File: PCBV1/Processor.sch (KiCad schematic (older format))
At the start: 41 parts

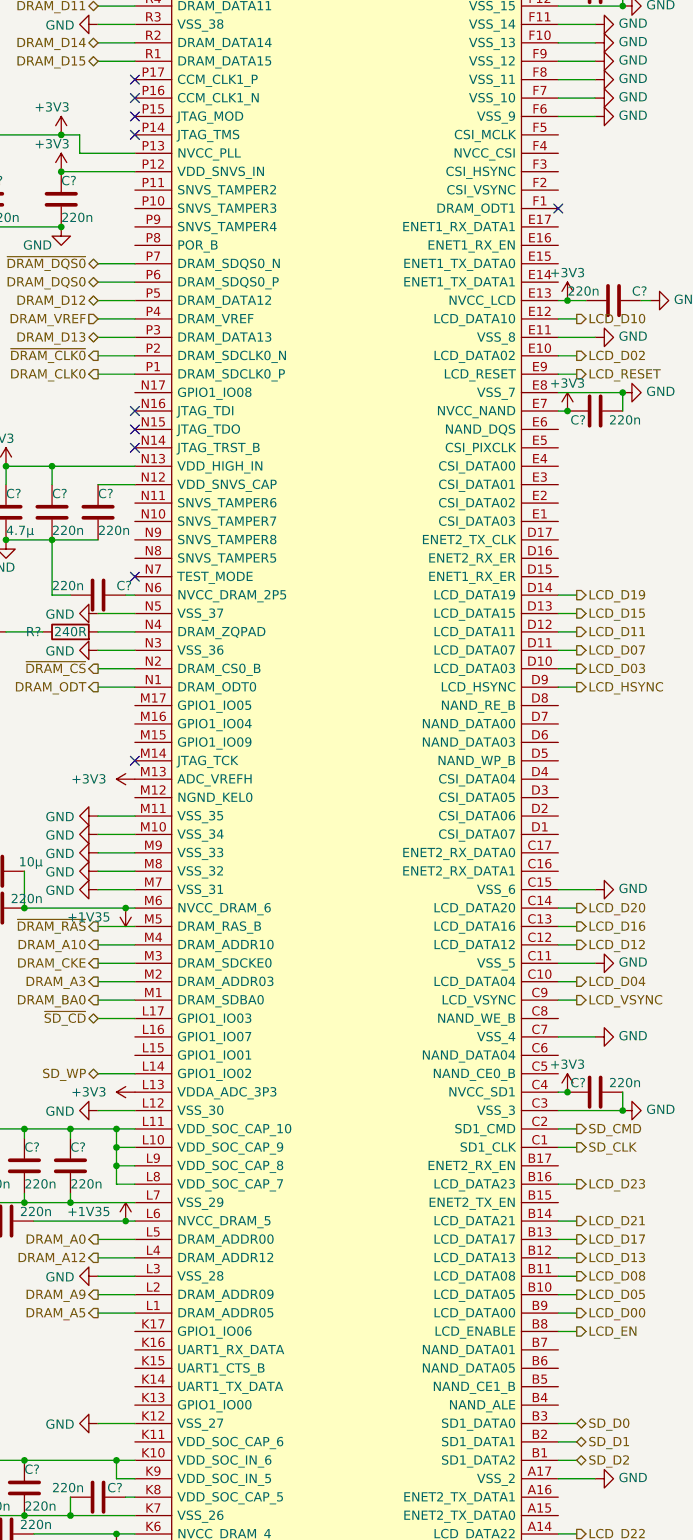
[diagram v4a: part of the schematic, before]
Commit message: Added SD filter and USB-to-UART IC.
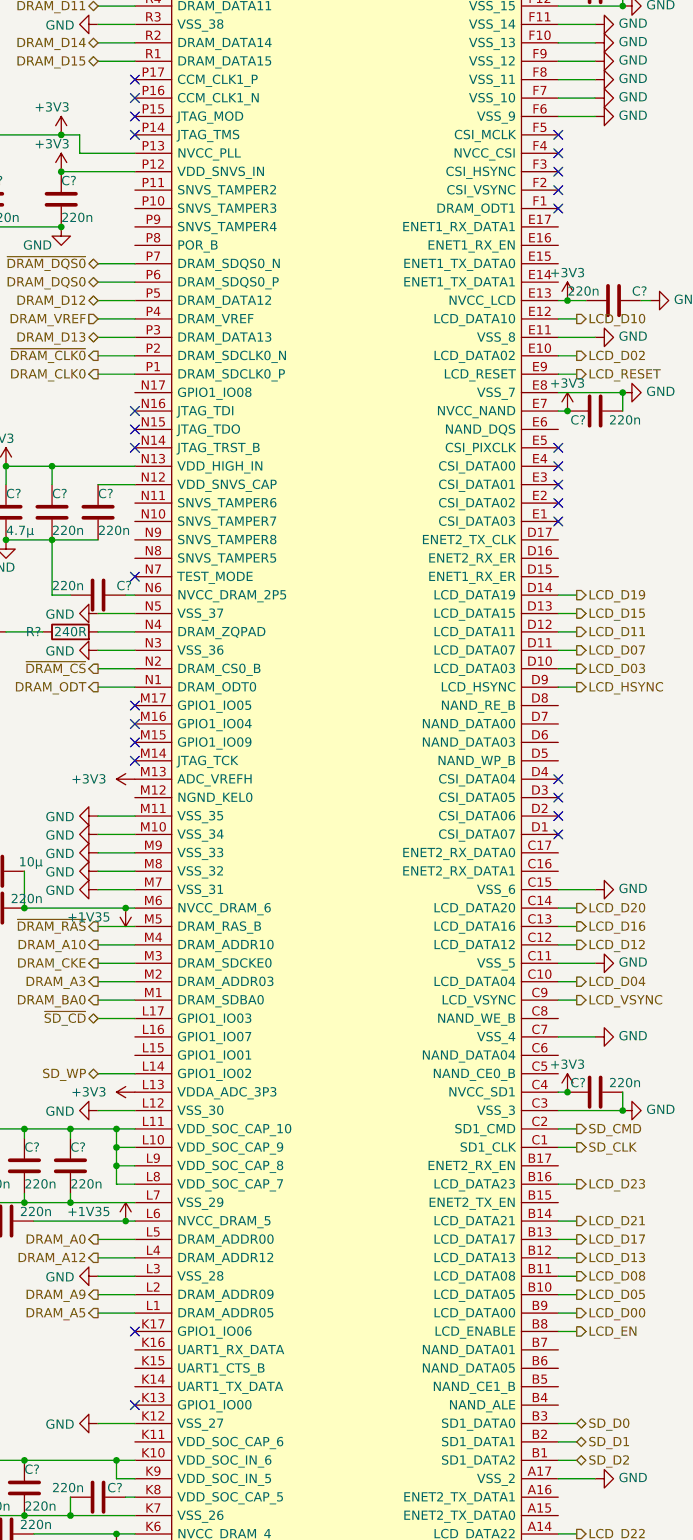
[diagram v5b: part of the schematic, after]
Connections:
- no-connect marks 21 -> 39
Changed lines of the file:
@@
 $Descr A3 11693 16535 portrait
 encoding utf-8
-Sheet 8 8
+Sheet 7 8
 Title "Smart Mirror"
-Date "2021-01-21"
+Date "2022-04-22"
 Rev "1.0"
 Comp "University of Southern Denmark"
@@
 	5150 7650 5050 7650
 NoConn ~ 5050 6750
+NoConn ~ 5050 10150
+NoConn ~ 5050 10050
+NoConn ~ 5050 9950
+NoConn ~ 5050 9850
+NoConn ~ 5050 8450
+NoConn ~ 5050 8350
+NoConn ~ 5050 8250
+NoConn ~ 5050 8150
+NoConn ~ 5050 8050
+NoConn ~ 5050 6650
+NoConn ~ 5050 6550
+NoConn ~ 5050 6450
+NoConn ~ 5050 6350
+NoConn ~ 2750 9450
+NoConn ~ 2750 9550
+NoConn ~ 2750 9650
+NoConn ~ 2750 13250
+NoConn ~ 2750 12850
 $EndSCHEMATC

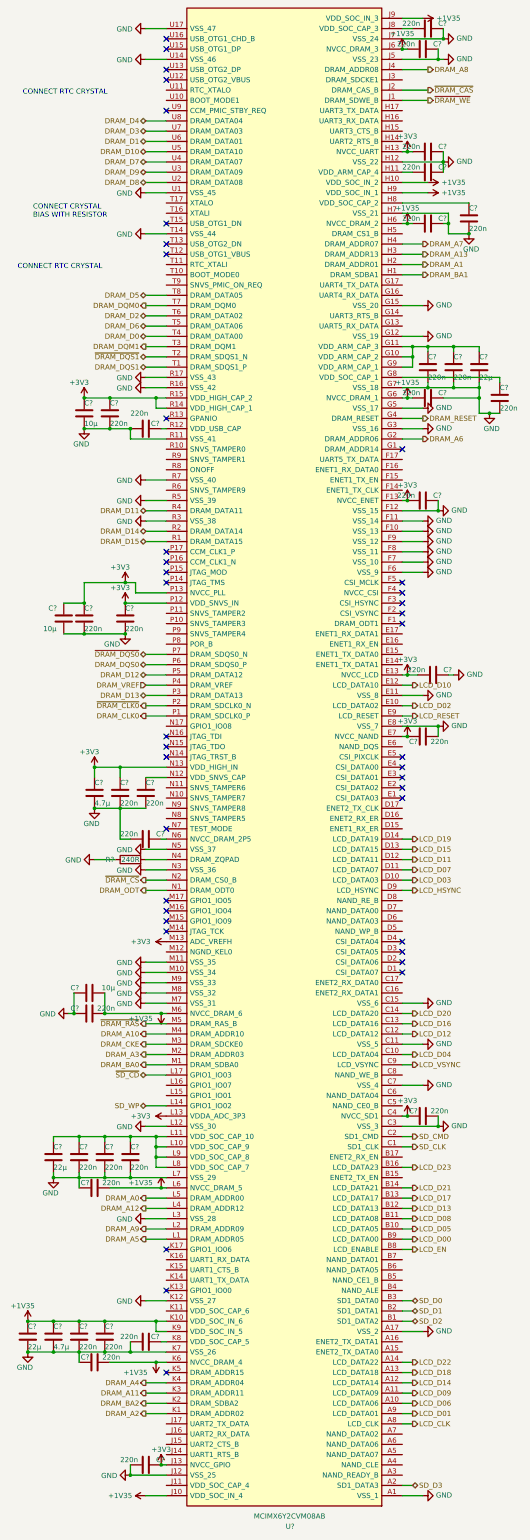
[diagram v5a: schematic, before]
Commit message: Many minor changes to component footprints and schematics.
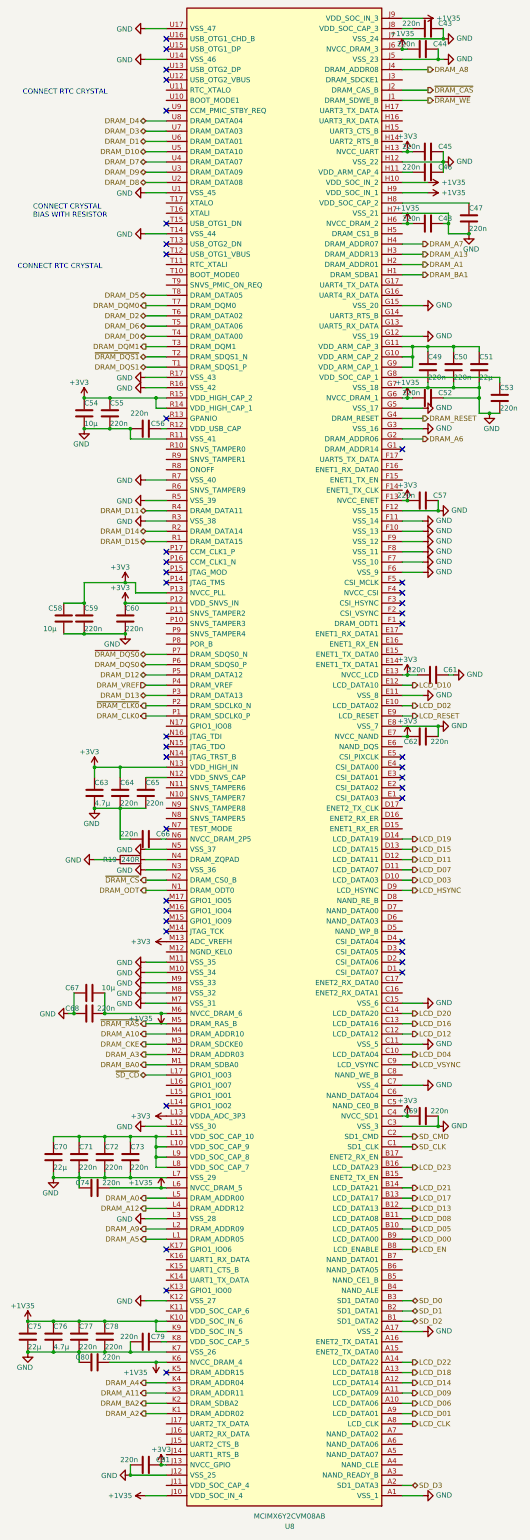
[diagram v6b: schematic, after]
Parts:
- C43, C44, C45, C46, C47, C48, C49, C50, C52, C53, C55, C56, C57, C59, C60, C61, C62, C64, C65, C66, C68, C69, C71, C72, C73, C74, C76, C77, C78, C79, C80, C81: renamed from C?; footprint (none) -> Capacitor_SMD:C_0603_1608Metric
- R19: renamed from R?; footprint (none) -> Resistor_SMD:R_0603_1608Metric
- gave numbers to parts that had none: 8
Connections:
- net SD_WP: no longer names the net of U8.L14 (GPIO1_IO02)
- no-connect marks 39 -> 40

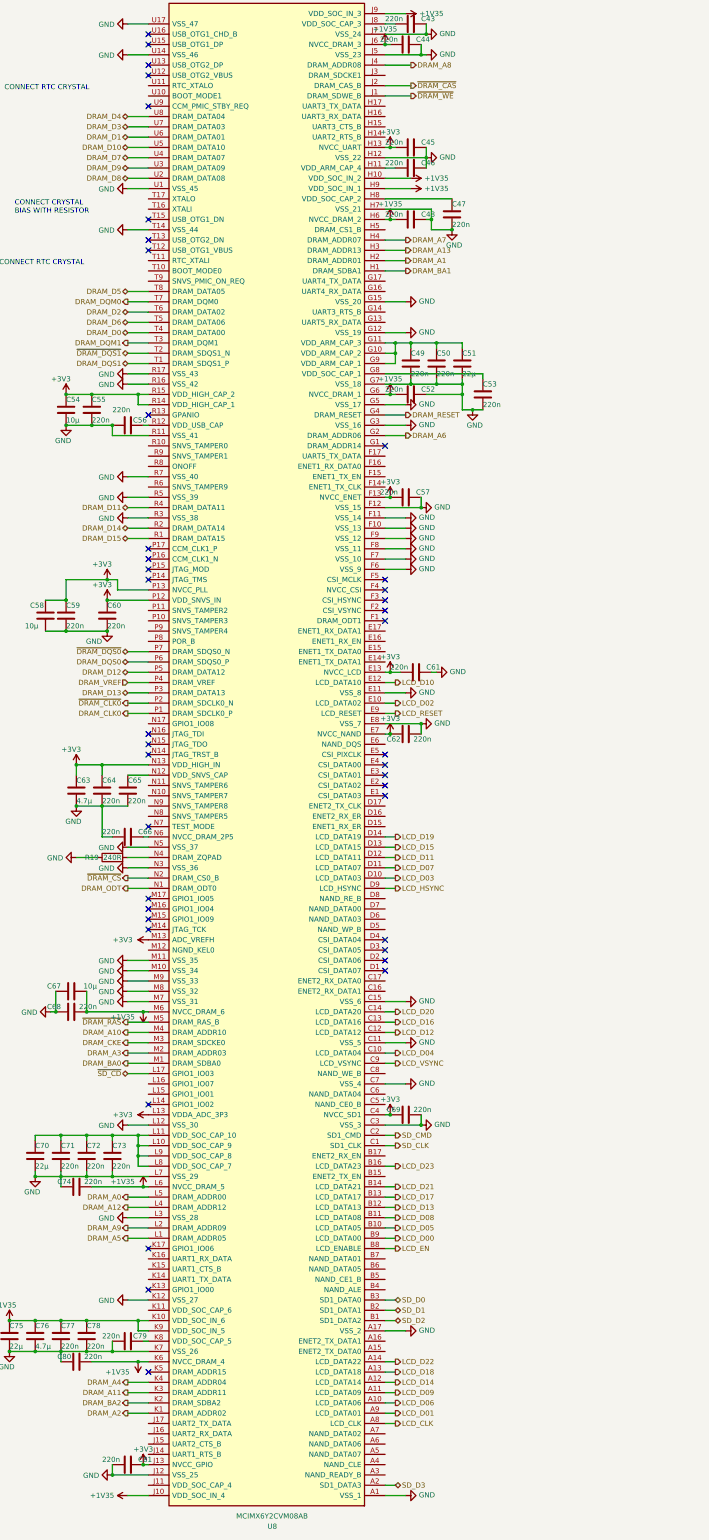
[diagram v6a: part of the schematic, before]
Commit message: Added NAND flash with connections, updated IO config.
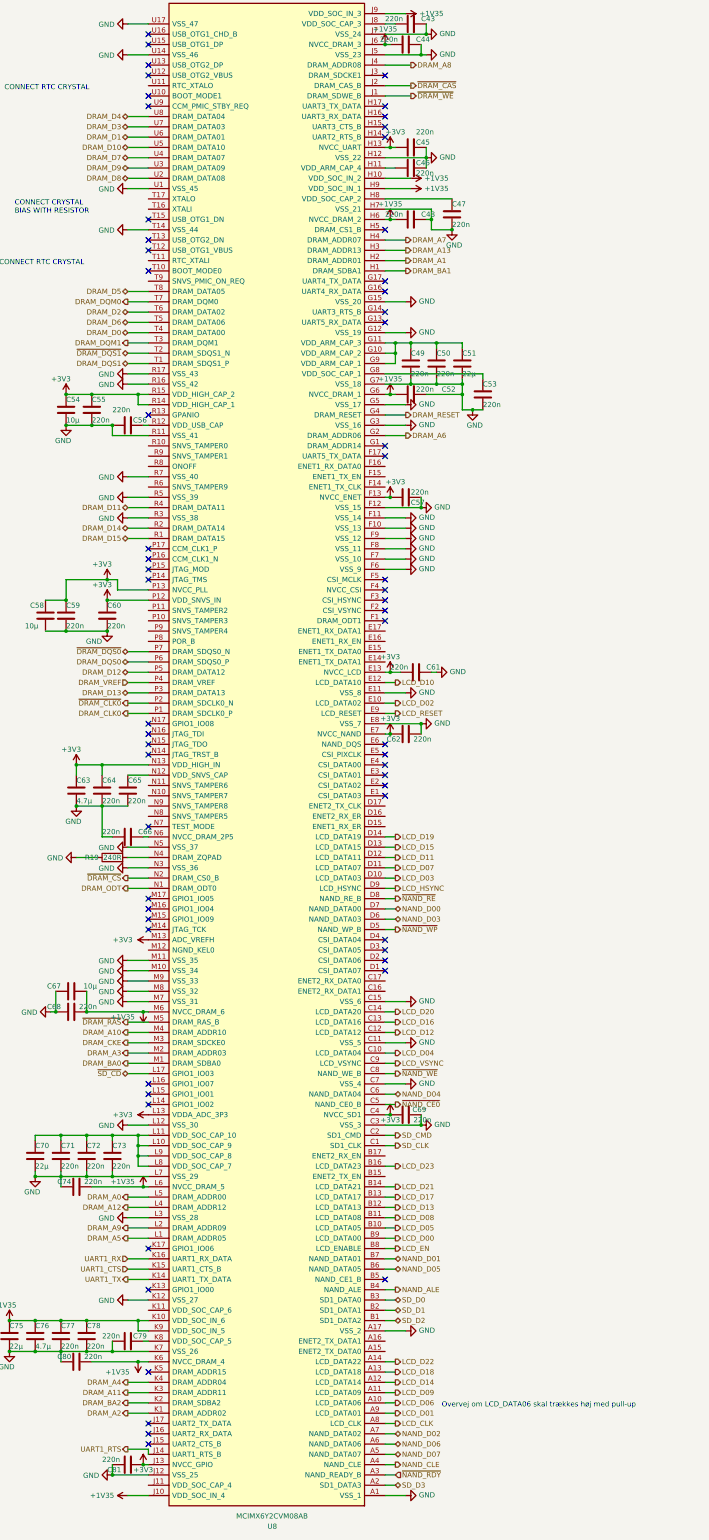
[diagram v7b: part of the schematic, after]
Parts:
- C51, C54, C58, C63, C67, C70, C75: footprint (none) -> Capacitor_SMD:C_0603_1608Metric
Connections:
- net ~NAND_RDY: now reaches U8.A3 (NAND_READY_B)
- net NAND_CLE: now reaches U8.A4 (NAND_CLE)
- net NAND_D07: now reaches U8.A5 (NAND_DATA07)
- net NAND_D06: now reaches U8.A6 (NAND_DATA06)
- net NAND_D02: now reaches U8.A7 (NAND_DATA02)
- net NAND_ALE: now reaches U8.B4 (NAND_ALE)
- net NAND_D05: now reaches U8.B6 (NAND_DATA05)
- net NAND_D01: now reaches U8.B7 (NAND_DATA01)
- net ~NAND_CE0: now reaches U8.C5 (NAND_CE0_B)
- net NAND_D04: now reaches U8.C6 (NAND_DATA04)
- net ~NAND_WE: now reaches U8.C8 (NAND_WE_B)
- net ~NAND_WP: now reaches U8.D5 (NAND_WP_B)
- net NAND_D03: now reaches U8.D6 (NAND_DATA03)
- net NAND_D00: now reaches U8.D7 (NAND_DATA00)
- net ~NAND_RE: now reaches U8.D8 (NAND_RE_B)
- net UART1_RTS: now reaches U8.J14 (UART1_RTS_B)
- net UART1_TX: now reaches U8.K14 (UART1_TX_DATA)
- net UART1_CTS: now reaches U8.K15 (UART1_CTS_B)
- net UART1_RX: now reaches U8.K16 (UART1_RX_DATA)
- no-connect marks 40 -> 61
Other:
- note added: "Overvej om LCD_DATA06 skal trækkes høj med pull-up"
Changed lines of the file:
@@
 F 0 "C75" H 1400 13800 50  0000 L CNN
 F 1 "22µ" H 1400 13600 50  0000 L CNN
-F 2 "" H 1438 13550 50  0001 C CNN
+F 2 "Capacitor_SMD:C_0603_1608Metric" H 1438 13550 50  0001 C CNN
 F 3 "~" H 1400 13700 50  0001 C CNN
 	1    1400 13700
@@
 F 0 "C51" H 5800 4350 50  0000 L CNN
 F 1 "22µ" H 5800 4150 50  0000 L CNN
-F 2 "" H 5838 4100 50  0001 C CNN
+F 2 "Capacitor_SMD:C_0603_1608Metric" H 5838 4100 50  0001 C CNN
 F 3 "~" H 5800 4250 50  0001 C CNN
 	1    5800 4250
@@
 F 0 "C70" H 1650 12050 50  0000 L CNN
 F 1 "22µ" H 1650 11850 50  0000 L CNN
-F 2 "" H 1688 11800 50  0001 C CNN
+F 2 "Capacitor_SMD:C_0603_1608Metric" H 1688 11800 50  0001 C CNN
 F 3 "~" H 1650 11950 50  0001 C CNN
 	1    1650 11950
@@
 F 0 "C63" H 2050 8500 50  0000 L CNN
 F 1 "4.7µ" H 2050 8300 50  0000 L CNN
-F 2 "" H 2088 8250 50  0001 C CNN
+F 2 "Capacitor_SMD:C_0603_1608Metric" H 2088 8250 50  0001 C CNN
 F 3 "~" H 2050 8400 50  0001 C CNN
 	1    2050 8400
@@
 F 0 "C54" H 1950 4800 50  0000 L CNN
 F 1 "10µ" H 1950 4600 50  0000 L CNN
-F 2 "" H 1988 4550 50  0001 C CNN
+F 2 "Capacitor_SMD:C_0603_1608Metric" H 1988 4550 50  0001 C CNN
 F 3 "~" H 1950 4700 50  0001 C CNN
 	1    1950 4700
@@
 F 0 "C58" H 1600 6800 50  0000 L CNN
 F 1 "10µ" H 1550 6600 50  0000 L CNN
-F 2 "" H 1788 6550 50  0001 C CNN
+F 2 "Capacitor_SMD:C_0603_1608Metric" H 1788 6550 50  0001 C CNN
 F 3 "~" H 1750 6700 50  0001 C CNN
 	1    1750 6700
@@
 Wire Wire Line
 	5500 2850 5500 2950
-$Comp
-L Device:C C52
-U 1 1 6142937F
-P 5300 4550
-F 0 "C52" V 5250 4650 50  0000 L CNN
-F 1 "220n" V 5250 4300 50  0000 L CNN
-F 2 "Capacitor_SMD:C_0603_1608Metric" H 5338 4400 50  0001 C CNN
-F 3 "~" H 5300 4550 50  0001 C CNN
-	1    5300 4550
-	0    1    1    0
-$EndComp
 Wire Wire Line
 	5450 4550 5800 4550
@@
 F 0 "C67" V 2050 10450 50  0000 L CNN
 F 1 "10µ" V 2050 10100 50  0000 L CNN
-F 2 "" H 2038 10200 50  0001 C CNN
+F 2 "Capacitor_SMD:C_0603_1608Metric" H 2038 10200 50  0001 C CNN
 F 3 "~" H 2000 10350 50  0001 C CNN
 	1    2000 10350
@@
 U 1 1 6149FCD3
 P 2550 14950
-F 0 "C81" V 2500 15050 50  0000 L CNN
+F 0 "C81" V 2600 14750 50  0000 L CNN
 F 1 "220n" V 2500 14700 50  0000 L CNN
 F 2 "Capacitor_SMD:C_0603_1608Metric" H 2588 14800 50  0001 C CNN
@@
 U 1 1 614CD7EE
 P 5250 11550
-F 0 "C69" V 5300 11600 50  0000 L CNN
-F 1 "220n" V 5300 11300 50  0000 L CNN
+F 0 "C69" V 5300 11350 50  0000 L CNN
+F 1 "220n" V 5200 11300 50  0000 L CNN
 F 2 "Capacitor_SMD:C_0603_1608Metric" H 5288 11400 50  0001 C CNN
 F 3 "~" H 5250 11550 50  0001 C CNN
@@
 U 1 1 6151BC34
 P 5250 5550
-F 0 "C57" V 5200 5650 50  0000 L CNN
-F 1 "220n" V 5200 5300 50  0000 L CNN
+F 0 "C57" V 5300 5600 50  0000 L CNN
+F 1 "220n" V 5200 5600 50  0000 L CNN
 F 2 "Capacitor_SMD:C_0603_1608Metric" H 5288 5400 50  0001 C CNN
 F 3 "~" H 5250 5550 50  0001 C CNN
@@
 U 1 1 615550B7
 P 5300 2350
-F 0 "C46" V 5250 2450 50  0000 L CNN
-F 1 "220n" V 5250 2100 50  0000 L CNN
+F 0 "C46" V 5250 2400 50  0000 L CNN
+F 1 "220n" V 5350 2400 50  0000 L CNN
 F 2 "Capacitor_SMD:C_0603_1608Metric" H 5338 2200 50  0001 C CNN
 F 3 "~" H 5300 2350 50  0001 C CNN
@@
 U 1 1 6158083A
 P 5300 2150
-F 0 "C45" V 5250 2250 50  0000 L CNN
-F 1 "220n" V 5250 1900 50  0000 L CNN
+F 0 "C45" V 5250 2200 50  0000 L CNN
+F 1 "220n" V 5150 2200 50  0000 L CNN
 F 2 "Capacitor_SMD:C_0603_1608Metric" H 5338 2000 50  0001 C CNN
 F 3 "~" H 5300 2150 50  0001 C CNN
@@
 P 5100 11550
 F 0 "#PWR0246" H 5100 11400 50  0001 C CNN
-F 1 "+3V3" H 5100 11700 50  0000 C CNN
+F 1 "+3V3" H 5100 11500 50  0000 C CNN
 F 2 "" H 5100 11550 50  0001 C CNN
 F 3 "" H 5100 11550 50  0001 C CNN
@@
 P 5100 2150
 F 0 "#PWR0247" H 5100 2000 50  0001 C CNN
-F 1 "+3V3" H 5100 2300 50  0000 C CNN
+F 1 "+3V3" H 5150 2300 50  0000 C CNN
 F 2 "" H 5100 2150 50  0001 C CNN
 F 3 "" H 5100 2150 50  0001 C CNN
@@
 P 5100 5550
 F 0 "#PWR0248" H 5100 5400 50  0001 C CNN
-F 1 "+3V3" H 5100 5700 50  0000 C CNN
+F 1 "+3V3" H 5150 5700 50  0000 C CNN
 F 2 "" H 5100 5550 50  0001 C CNN
 F 3 "" H 5100 5550 50  0001 C CNN
@@
 P 2700 14950
 F 0 "#PWR0251" H 2700 14800 50  0001 C CNN
-F 1 "+3V3" H 2700 15100 50  0000 C CNN
+F 1 "+3V3" H 2700 14900 50  0000 C CNN
 F 2 "" H 2700 14950 50  0001 C CNN
 F 3 "" H 2700 14950 50  0001 C CNN
@@
 NoConn ~ 2750 12850
 NoConn ~ 2750 11450
+Wire Wire Line
+	2750 14850 2750 14800
+Wire Wire Line
+	2750 14800 2550 14800
+Text HLabel 2550 14800 0    50   Output ~ 0
+UART1_RTS
+NoConn ~ 2750 14750
+NoConn ~ 2750 14650
+NoConn ~ 2750 14550
+Wire Wire Line
+	2750 13150 2550 13150
+Wire Wire Line
+	2550 13050 2750 13050
+Wire Wire Line
+	2750 12950 2550 12950
+Text HLabel 2550 13150 0    50   Output ~ 0
+UART1_TX
+Text HLabel 2550 12950 0    50   Input ~ 0
+UART1_RX
+Text HLabel 2550 13050 0    50   Input ~ 0
+UART1_CTS
+NoConn ~ 2750 11250
+NoConn ~ 2750 11350
+NoConn ~ 2750 7750
+NoConn ~ 5050 1750
+NoConn ~ 5050 1850
+NoConn ~ 5050 1950
+NoConn ~ 5050 2050
+NoConn ~ 5050 1450
+NoConn ~ 5050 2950
+NoConn ~ 5050 3450
+NoConn ~ 5050 3550
+NoConn ~ 5050 3750
+NoConn ~ 5050 3850
+$Comp
+L Device:C C52
+U 1 1 6142937F
+P 5300 4550
+F 0 "C52" V 5250 4850 50  0000 L CNN
+F 1 "220n" V 5250 4600 50  0000 L CNN
+F 2 "Capacitor_SMD:C_0603_1608Metric" H 5338 4400 50  0001 C CNN
+F 3 "~" H 5300 4550 50  0001 C CNN
+	1    5300 4550
+	0    1    1    0
+$EndComp
+NoConn ~ 5050 5150
+Text Notes 5600 14400 0    50   ~ 0
+Overvej om LCD_DATA06 skal trækkes høj med pull-up
+NoConn ~ 2750 3350
+NoConn ~ 2750 1650
+Wire Wire Line
+	5050 14850 5150 14850
+Text HLabel 5150 14850 2    50   BiDi ~ 0
+NAND_D07
+Text HLabel 5150 14750 2    50   BiDi ~ 0
+NAND_D06
+Text HLabel 5150 14650 2    50   BiDi ~ 0
+NAND_D02
+Wire Wire Line
+	5050 14650 5150 14650
+Wire Wire Line
+	5050 14750 5150 14750
+Wire Wire Line
+	5050 14950 5150 14950
+Text HLabel 5150 14950 2    50   Output ~ 0
+NAND_CLE
+Wire Wire Line
+	5050 15050 5150 15050
+Text HLabel 5150 15050 2    50   Input ~ 0
+~NAND_RDY
+Wire Wire Line
+	5050 13250 5150 13250
+Text HLabel 5150 13250 2    50   Output ~ 0
+NAND_ALE
+NoConn ~ 5050 13150
+Text HLabel 5150 13050 2    50   BiDi ~ 0
+NAND_D05
+Wire Wire Line
+	5150 13050 5050 13050
+Text HLabel 5150 12950 2    50   BiDi ~ 0
+NAND_D01
+Wire Wire Line
+	5050 12950 5150 12950
+Wire Wire Line
+	5050 11450 5150 11450
+Text HLabel 5150 11450 2    50   Output ~ 0
+~NAND_CE0
+Wire Wire Line
+	5050 11350 5150 11350
+Text HLabel 5150 11350 2    50   BiDi ~ 0
+NAND_D04
+Wire Wire Line
+	5050 11150 5150 11150
+Text HLabel 5150 11150 2    50   Output ~ 0
+~NAND_WE
+Wire Wire Line
+	5050 9750 5150 9750
+Text HLabel 5150 9750 2    50   Output ~ 0
+~NAND_WP
+Wire Wire Line
+	5050 9650 5150 9650
+Text HLabel 5150 9650 2    50   BiDi ~ 0
+NAND_D03
+Text HLabel 5150 9550 2    50   BiDi ~ 0
+NAND_D00
+Wire Wire Line
+	5050 9550 5150 9550
+Wire Wire Line
+	5050 9450 5150 9450
+Text HLabel 5150 9450 2    50   Output ~ 0
+~NAND_RE
+NoConn ~ 5050 7950
 $EndSCHEMATC
